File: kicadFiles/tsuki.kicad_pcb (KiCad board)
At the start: 2 copper layers, 283 x 94.2 mm, 194 parts, among them J1 TYPE-C-31-M12_13, J2 Conn_01x14, J3 Conn_01x14, SW1 ESC, SW10 9, SW11 0, SW12 -_, SW13 +=, SW14 2U BKSP, SW15 TAB_150, SW16 Q, SW17 W, SW18 E, SW19 R, SW2 1, SW20 T, SW21 Y, SW22 U, SW23 I, SW24 O, SW25 P, SW26 [{, SW27 ]}, SW28 \|_150, SW29 CAPS_175, SW3 2, SW30 A, SW31 S, SW32 D, SW33 F, SW34 G, SW35 H, SW36 J, SW37 K, SW38 L, SW39 :;, SW4 3, SW40 "', SW41 ENTER_225, SW42 LSHIFT_225, SW43 Z, SW44 X, SW45 C, SW46 V, SW47 B, SW48 N, SW49 M, SW5 4, SW50 <,, SW51 >., SW52 ?/, SW53 RSHIFT_275, SW54 LCTRL_150, SW55 LGUI_100, SW56 LALT_150, SW57 SPACE_600, SW58 RALT_150, SW59 RGUI_150, SW6 5, SW60 RCTRL_150, SW61 FN_100, SW62 RSHIFT_175, SW63 STEPPED_CAPS_125, SW64 1U LBKSP, SW65 1U RBKSP, SW66 ISO_100, SW67 ISO_ENTER, SW68 LCTRL_125, SW69 LGUI_125, SW7 6, SW70 LGUI_100, SW71 LALT_125, SW72 LALT_150, SW75 SPACE_625, SW77 SPACE_700, SW8 7, SW80 RALT_125, SW81 RALT_150, SW83 RGUI_125, SW84 RGUI_100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

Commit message: Added Schottky diodes and TVS
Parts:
- moved L4 20.3 mm to (250.9, 187.9)
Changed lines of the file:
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@@
     (mod_text_size 1 1)
     (mod_text_width 0.15)
-    (pad_size 3.9878 3.9878)
-    (pad_drill 3.9878)
+    (pad_size 10 4.500001)
+    (pad_drill 7.999999)
     (pad_to_mask_clearance 0.051)
     (solder_mask_min_width 0.25)
@@
     (fp_line (start -6 0) (end 6 0) (layer Cmts.User) (width 0.1))
     (fp_line (start 0 4) (end 0 -4) (layer Cmts.User) (width 0.1))
-    (pad "" thru_hole oval (at 0 0) (size 10 4.5) (drill oval 8 2.5) (layers *.Cu *.Mask))
+    (pad "" thru_hole oval (at 0 0) (size 10 4.500001) (drill oval 7.999999 2.5) (layers *.Cu *.Mask)
+      (clearance 1.016))
   )
   (module acheron_MountingHoles:MoutingHole_Oval_BackOnly_7mm_5.0x2.5mm (layer B.Cu)
@@
   )
   (module tsukiGraphics:tsukiLabel_30x12mm (layer F.Cu)
-    (at 250.92625 167.553125)
+    (at 250.92625 187.873125)
     (fp_text reference L4 (at 0 0) (layer F.Cu) hide
       (effects (font (size 1.524 1.524) (thickness 0.3)))
@@
   (module acheron_MountingHoles:MoutingHole_Oval_7mm_5.0x2.5mm (layer F.Cu)
     (at 279.50097 91.353125)
+    (clearance 1.016)
     (attr virtual)
     (fp_text reference H8 (at 0.1753 5.7861) (layer F.SilkS) hide
@@
     (fp_line (start -6 0) (end 6 0) (layer Cmts.User) (width 0.1))
     (fp_line (start 0 4) (end 0 -4) (layer Cmts.User) (width 0.1))
-    (pad "" thru_hole oval (at 0 0 180) (size 10 4.5) (drill oval 8 2.5) (layers *.Cu *.Mask))
+    (pad "" thru_hole oval (at 0 0 180) (size 10 4.500001) (drill oval 7.999999 2.5) (layers *.Cu *.Mask)
+      (clearance 1.016))
   )
   (module acheron_Components:D_SOD-123 (layer F.Cu)

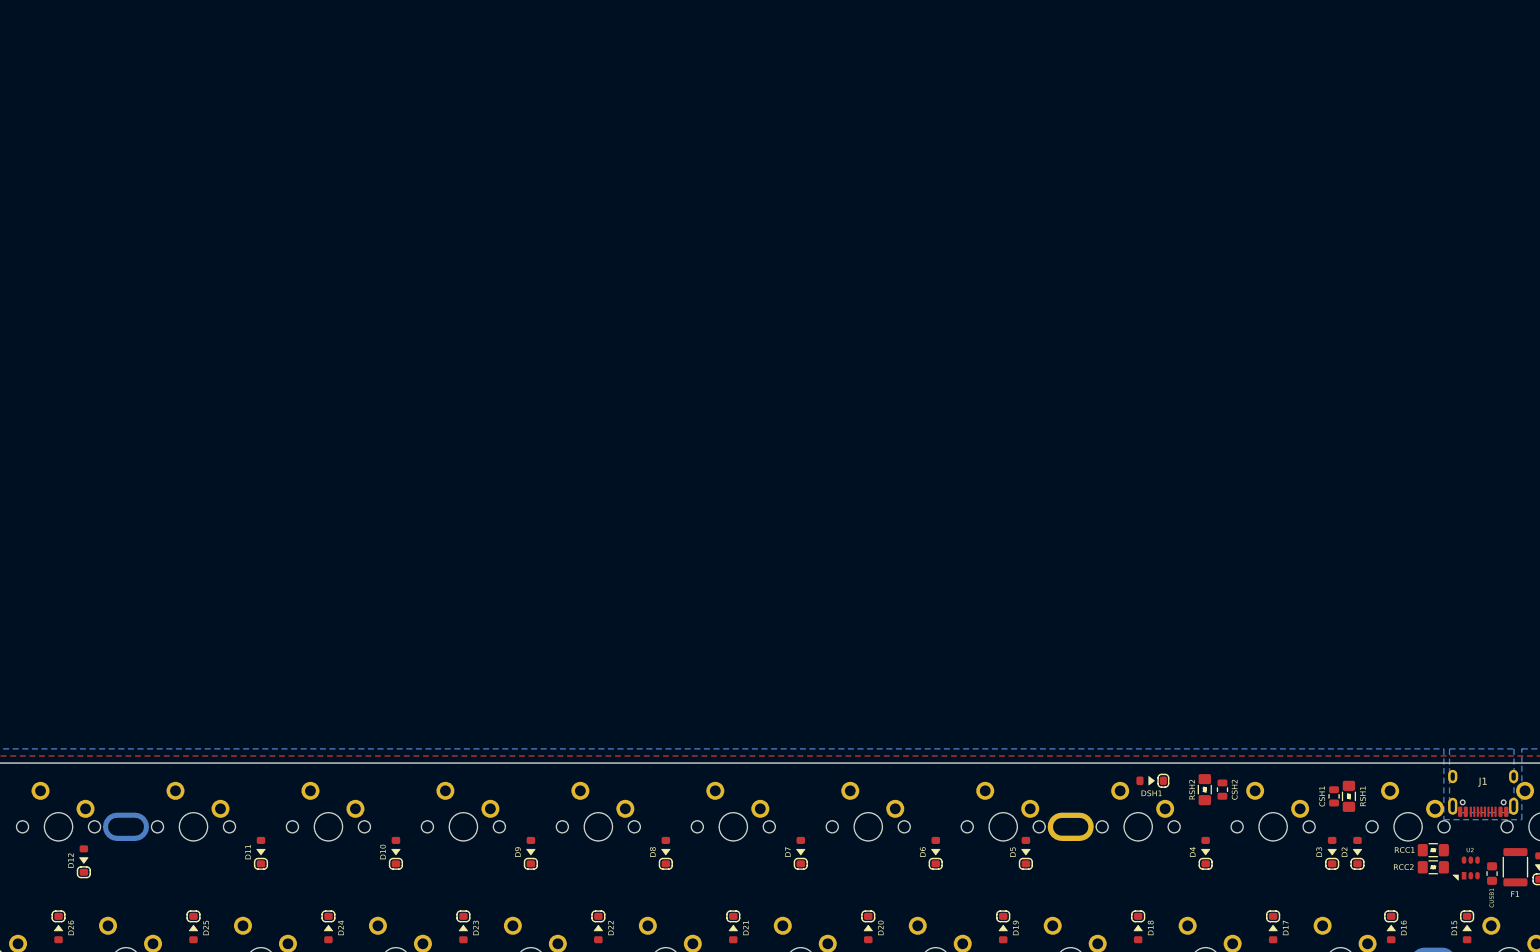
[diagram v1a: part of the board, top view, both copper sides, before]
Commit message: Added RGB to schematic
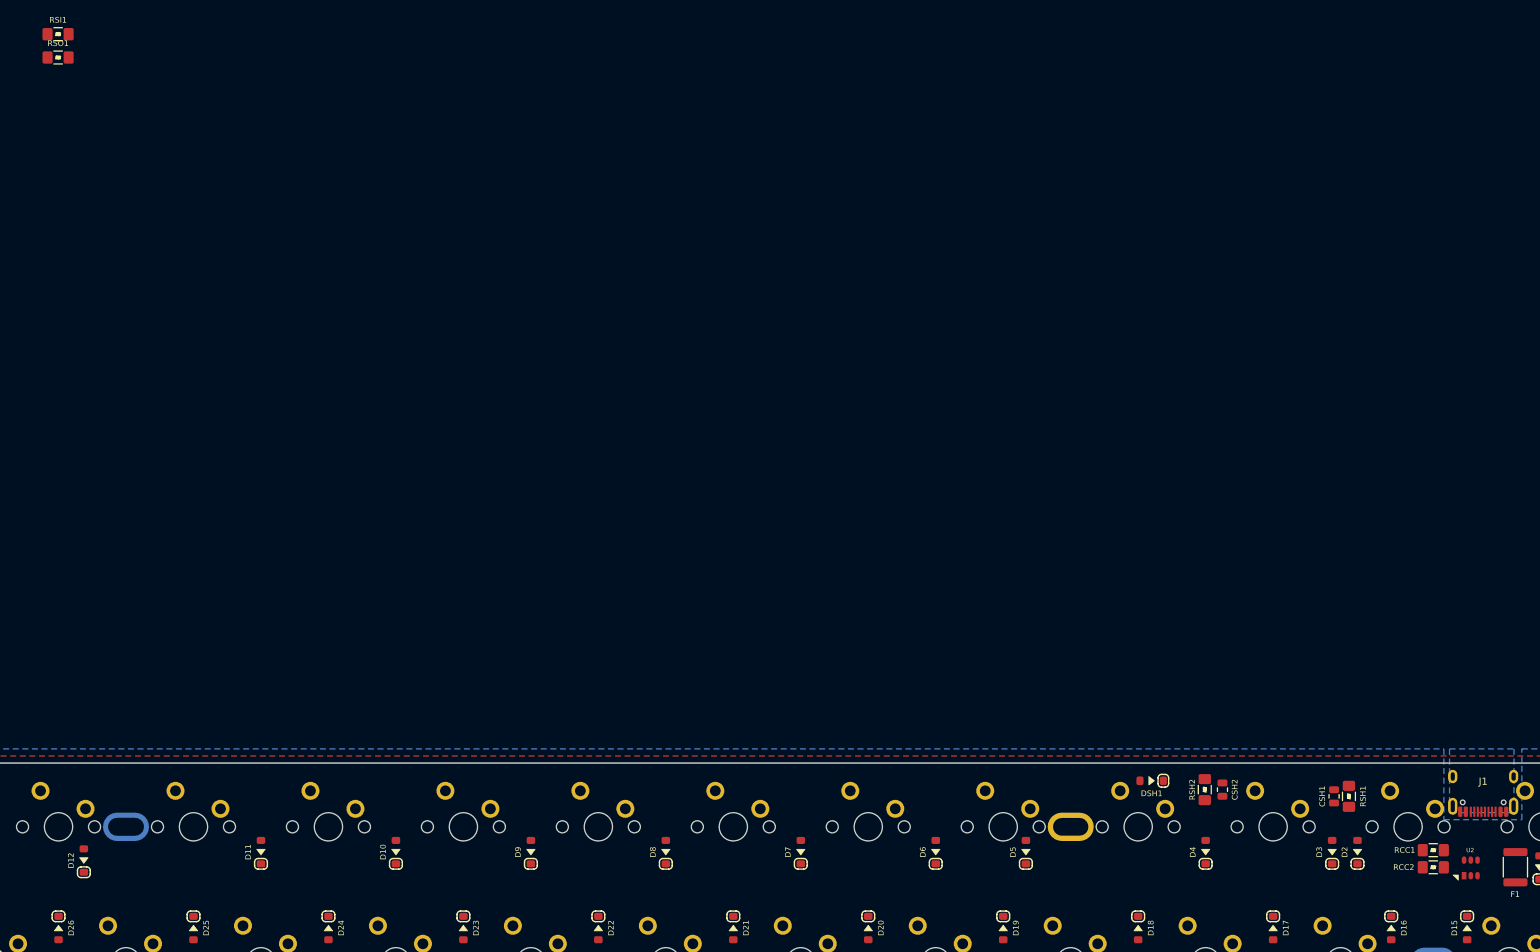
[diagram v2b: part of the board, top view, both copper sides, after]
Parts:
- removed CUSB1: 100n, Capacitor_SMD:C_0805_2012Metric_Pad1.15x1.40mm_HandSolder
- added RSI1: 100k, acheron_Components:R_SMD_1206, F.Cu at (136.6, -20.5)
- added RSO1: 100k, acheron_Components:R_SMD_1206, F.Cu at (136.6, -17.2)
- CSI1, CSO1: value 100n -> 1u
- DF1: value RB060M-60TR -> SMF9.0CA
- DS1: value 1N4148 -> RB060M-60TR
- DSH1: value 1N4007 -> RB060M-60TR
- J3: value Conn_01x14 -> Conn_ARM_JTAG_SWD_10
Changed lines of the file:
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@@
     (tracks 0)
     (zones 0)
-    (modules 194)
+    (modules 195)
     (nets 122)
   )
@@
     (add_net D-)
   )
+  (module acheron_Components:R_SMD_1206 (layer F.Cu)
+    (at 136.561251 -17.241874)
+    (descr "Resistor SMD 1206 (3216 Metric), square (rectangular) end terminal, IPC_7351 nominal with elongated pad for handsoldering. (Body size source: http://www.tortai-tech.com/upload/download/2011102023233369053.pdf), generated with kicad-footprint-generator")
+    (tags "resistor handsolder")
+    (attr smd)
+    (fp_text reference RSO1 (at 0 -2) (layer F.SilkS)
+      (effects (font (size 0.8 0.8) (thickness 0.2)))
+    )
+    (fp_text value 100k (at 0 2) (layer F.Fab)
+      (effects (font (size 0.6 0.6) (thickness 0.1)))
+    )
+    (fp_line (start 0.25 0.2) (end 0.35 -0.2) (layer F.SilkS) (width 0.1))
+    (fp_line (start 0.15 -0.2) (end 0.25 0.2) (layer F.SilkS) (width 0.1))
+    (fp_line (start 0.05 0.2) (end 0.15 -0.2) (layer F.SilkS) (width 0.1))
+    (fp_line (start -0.05 -0.2) (end 0.05 0.2) (layer F.SilkS) (width 0.1))
+    (fp_line (start -0.15 0.2) (end -0.05 -0.2) (layer F.SilkS) (width 0.1))
+    (fp_line (start -0.25 -0.2) (end -0.15 0.2) (layer F.SilkS) (width 0.1))
+    (fp_line (start -0.35 0.2) (end -0.25 -0.2) (layer F.SilkS) (width 0.1))
+    (fp_text user %R (at 0 0) (layer F.Fab)
+      (effects (font (size 0.6 0.6) (thickness 0.15)))
+    )
+    (fp_line (start 2.45 1.12) (end -2.45 1.12) (layer F.CrtYd) (width 0.05))
+    (fp_line (start 2.45 -1.12) (end 2.45 1.12) (layer F.CrtYd) (width 0.05))
+    (fp_line (start -2.45 -1.12) (end 2.45 -1.12) (layer F.CrtYd) (width 0.05))
+    (fp_line (start -2.45 1.12) (end -2.45 -1.12) (layer F.CrtYd) (width 0.05))
+    (fp_line (start -0.602064 0.91) (end 0.602064 0.91) (layer F.SilkS) (width 0.12))
+    (fp_line (start -0.602064 -0.91) (end 0.602064 -0.91) (layer F.SilkS) (width 0.12))
+    (fp_line (start 1.6 0.8) (end -1.6 0.8) (layer F.Fab) (width 0.1))
+    (fp_line (start 1.6 -0.8) (end 1.6 0.8) (layer F.Fab) (width 0.1))
+    (fp_line (start -1.6 -0.8) (end 1.6 -0.8) (layer F.Fab) (width 0.1))
+    (fp_line (start -1.6 0.8) (end -1.6 -0.8) (layer F.Fab) (width 0.1))
+    (pad 2 smd roundrect (at 1.4875 0) (size 1.425 1.75) (layers F.Cu F.Paste F.Mask) (roundrect_rratio 0.175439)
+      (net 2 GND))
+    (pad 1 smd roundrect (at -1.4875 0) (size 1.425 1.75) (layers F.Cu F.Paste F.Mask) (roundrect_rratio 0.175439)
+      (net 1 3.3V))
+    (model ${KISYS3DMOD}/Resistor_SMD.3dshapes/R_1206_3216Metric.wrl
+      (at (xyz 0 0 0))
+      (scale (xyz 1 1 1))
+      (rotate (xyz 0 0 0))
+    )
+  )
+  (module acheron_Components:R_SMD_1206 (layer F.Cu)
+    (at 136.561251 -20.531874)
+    (descr "Resistor SMD 1206 (3216 Metric), square (rectangular) end terminal, IPC_7351 nominal with elongated pad for handsoldering. (Body size source: http://www.tortai-tech.com/upload/download/2011102023233369053.pdf), generated with kicad-footprint-generator")
+    (tags "resistor handsolder")
+    (attr smd)
+    (fp_text reference RSI1 (at 0 -2) (layer F.SilkS)
+      (effects (font (size 0.8 0.8) (thickness 0.2)))
+    )
+    (fp_text value 100k (at 0 2) (layer F.Fab)
+      (effects (font (size 0.6 0.6) (thickness 0.1)))
+    )
+    (fp_line (start 0.25 0.2) (end 0.35 -0.2) (layer F.SilkS) (width 0.1))
+    (fp_line (start 0.15 -0.2) (end 0.25 0.2) (layer F.SilkS) (width 0.1))
+    (fp_line (start 0.05 0.2) (end 0.15 -0.2) (layer F.SilkS) (width 0.1))
+    (fp_line (start -0.05 -0.2) (end 0.05 0.2) (layer F.SilkS) (width 0.1))
+    (fp_line (start -0.15 0.2) (end -0.05 -0.2) (layer F.SilkS) (width 0.1))
+    (fp_line (start -0.25 -0.2) (end -0.15 0.2) (layer F.SilkS) (width 0.1))
+    (fp_line (start -0.35 0.2) (end -0.25 -0.2) (layer F.SilkS) (width 0.1))
+    (fp_text user %R (at 0 0) (layer F.Fab)
+      (effects (font (size 0.6 0.6) (thickness 0.15)))
+    )
+    (fp_line (start 2.45 1.12) (end -2.45 1.12) (layer F.CrtYd) (width 0.05))
+    (fp_line (start 2.45 -1.12) (end 2.45 1.12) (layer F.CrtYd) (width 0.05))
+    (fp_line (start -2.45 -1.12) (end 2.45 -1.12) (layer F.CrtYd) (width 0.05))
+    (fp_line (start -2.45 1.12) (end -2.45 -1.12) (layer F.CrtYd) (width 0.05))
+    (fp_line (start -0.602064 0.91) (end 0.602064 0.91) (layer F.SilkS) (width 0.12))
+    (fp_line (start -0.602064 -0.91) (end 0.602064 -0.91) (layer F.SilkS) (width 0.12))
+    (fp_line (start 1.6 0.8) (end -1.6 0.8) (layer F.Fab) (width 0.1))
+    (fp_line (start 1.6 -0.8) (end 1.6 0.8) (layer F.Fab) (width 0.1))
+    (fp_line (start -1.6 -0.8) (end 1.6 -0.8) (layer F.Fab) (width 0.1))
+    (fp_line (start -1.6 0.8) (end -1.6 -0.8) (layer F.Fab) (width 0.1))
+    (pad 2 smd roundrect (at 1.4875 0) (size 1.425 1.75) (layers F.Cu F.Paste F.Mask) (roundrect_rratio 0.175439)
+      (net 2 GND))
+    (pad 1 smd roundrect (at -1.4875 0) (size 1.425 1.75) (layers F.Cu F.Paste F.Mask) (roundrect_rratio 0.175439)
+      (net 6 5V))
+    (model ${KISYS3DMOD}/Resistor_SMD.3dshapes/R_1206_3216Metric.wrl
+      (at (xyz 0 0 0))
+      (scale (xyz 1 1 1))
+      (rotate (xyz 0 0 0))
+    )
+  )
   (module acheron_MountingHoles:MoutingHole_Oval_BackOnly_7mm_5.0x2.5mm (layer B.Cu)
     (at 95.32625 110.403205 180)
@@
       (effects (font (size 1 1) (thickness 0.15)))
     )
-    (fp_text value Conn_01x14 (at 4.064 0 90) (layer F.Fab) hide
+    (fp_text value Conn_ARM_JTAG_SWD_10 (at 4.064 0 90) (layer F.Fab) hide
       (effects (font (size 1 1) (thickness 0.15)))
     )
@@
       (effects (font (size 0.8 0.8) (thickness 0.2)))
     )
-    (fp_text value 1N4007 (at 0 1.524) (layer F.Fab)
+    (fp_text value RB060M-60TR (at 0 1.524) (layer F.Fab)
       (effects (font (size 0.5 0.5) (thickness 0.125)))
     )
@@
       (effects (font (size 0.8 0.8) (thickness 0.2)))
     )
-    (fp_text value 1N4148 (at 0 2.41 90) (layer F.Fab)
+    (fp_text value RB060M-60TR (at 0 2.41 90) (layer F.Fab)
       (effects (font (size 0.5 0.5) (thickness 0.125)))
     )
@@
       (effects (font (size 0.8 0.8) (thickness 0.2)))
     )
-    (fp_text value RB060M-60TR (at 0 1.524 90) (layer F.Fab)
+    (fp_text value SMF9.0CA (at 0 1.524 90) (layer F.Fab)
       (effects (font (size 0.5 0.5) (thickness 0.125)))
     )
@@
   )
   (module Capacitor_SMD:C_0805_2012Metric_Pad1.15x1.40mm_HandSolder (layer F.Cu)
-    (at 338.97625 97.953125 90)
-    (descr "Capacitor SMD 0805 (2012 Metric), square (rectangular) end terminal, IPC_7351 nominal with elongated pad for handsoldering. (Body size source: https://docs.google.com/spreadsheets/d/1BsfQQcO9C6DZCsRaXUlFlo91Tg2WpOkGARC1WS5S8t0/edit?usp=sharing), generated with kicad-footprint-generator")
-    (tags "capacitor handsolder")
-    (attr smd)
-    (fp_text reference CUSB1 (at -3.433 -0.039 90) (layer F.SilkS)
-      (effects (font (size 0.6 0.6) (thickness 0.12)))
-    )
-    (fp_text value 100n (at -2.036 0.088 90) (layer F.Fab)
-      (effects (font (size 0.5 0.5) (thickness 0.1)))
-    )
-    (fp_text user %R (at 0 0 90) (layer F.Fab)
-      (effects (font (size 0.3 0.3) (thickness 0.075)))
-    )
-    (fp_line (start 1.85 0.95) (end -1.85 0.95) (layer F.CrtYd) (width 0.05))
-    (fp_line (start 1.85 -0.95) (end 1.85 0.95) (layer F.CrtYd) (width 0.05))
-    (fp_line (start -1.85 -0.95) (end 1.85 -0.95) (layer F.CrtYd) (width 0.05))
-    (fp_line (start -1.85 0.95) (end -1.85 -0.95) (layer F.CrtYd) (width 0.05))
-    (fp_line (start -0.261252 0.71) (end 0.261252 0.71) (layer F.SilkS) (width 0.12))
-    (fp_line (start -0.261252 -0.71) (end 0.261252 -0.71) (layer F.SilkS) (width 0.12))
-    (fp_line (start 1 0.6) (end -1 0.6) (layer F.Fab) (width 0.1))
-    (fp_line (start 1 -0.6) (end 1 0.6) (layer F.Fab) (width 0.1))
-    (fp_line (start -1 -0.6) (end 1 -0.6) (layer F.Fab) (width 0.1))
-    (fp_line (start -1 0.6) (end -1 -0.6) (layer F.Fab) (width 0.1))
-    (pad 2 smd roundrect (at 1.025 0 90) (size 1.15 1.4) (layers F.Cu F.Paste F.Mask) (roundrect_rratio 0.217391)
-      (net 7 VBUS))
-    (pad 1 smd roundrect (at -1.025 0 90) (size 1.15 1.4) (layers F.Cu F.Paste F.Mask) (roundrect_rratio 0.217391)
-      (net 2 GND))
-    (model ${KISYS3DMOD}/Capacitor_SMD.3dshapes/C_0805_2012Metric.wrl
-      (at (xyz 0 0 0))
-      (scale (xyz 1 1 1))
-      (rotate (xyz 0 0 0))
-    )
-  )
-  (module Capacitor_SMD:C_0805_2012Metric_Pad1.15x1.40mm_HandSolder (layer F.Cu)
     (at 318.87625 153.353125 180)
     (descr "Capacitor SMD 0805 (2012 Metric), square (rectangular) end terminal, IPC_7351 nominal with elongated pad for handsoldering. (Body size source: https://docs.google.com/spreadsheets/d/1BsfQQcO9C6DZCsRaXUlFlo91Tg2WpOkGARC1WS5S8t0/edit?usp=sharing), generated with kicad-footprint-generator")
@@
       (effects (font (size 0.6 0.6) (thickness 0.12)))
     )
-    (fp_text value 100n (at 0 -1.246) (layer F.Fab)
+    (fp_text value 1u (at 0 -1.246) (layer F.Fab)
       (effects (font (size 0.5 0.5) (thickness 0.1)))
     )
@@
       (effects (font (size 0.6 0.6) (thickness 0.12)))
     )
-    (fp_text value 100n (at 0 -1.368) (layer F.Fab)
+    (fp_text value 1u (at 0 -1.368) (layer F.Fab)
       (effects (font (size 0.5 0.5) (thickness 0.1)))
     )

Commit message: Added LED control to schematic
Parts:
- removed SW57: SPACE_600, acheron_MX_SolderMask:MX600R
- added CRGB1: 100n, Capacitor_SMD:C_0805_2012Metric, F.Cu at (303.3, 100.9)
- added CRGB10: 100n, Capacitor_SMD:C_0805_2012Metric, F.Cu at (470.6, 187.0)
- added CRGB2: 100n, Capacitor_SMD:C_0805_2012Metric, F.Cu at (256.6, 101.6)
- added CRGB3: 100n, Capacitor_SMD:C_0805_2012Metric, F.Cu at (466.6, 196.6)
- added CRGB4: 100n, Capacitor_SMD:C_0805_2012Metric, F.Cu at (462.2, 201.1)
- added CRGB5: 100n, Capacitor_SMD:C_0805_2012Metric, F.Cu at (471.1, 190.0)
- added CRGB6: 100n, Capacitor_SMD:C_0805_2012Metric, F.Cu at (466.7, 193.6)
- added CRGB7: 100n, Capacitor_SMD:C_0805_2012Metric, F.Cu at (462.2, 198.2)
- added CRGB8: 100n, Capacitor_SMD:C_0805_2012Metric, F.Cu at (462.2, 195.2)
- added CRGB9: 100n, Capacitor_SMD:C_0805_2012Metric, F.Cu at (466.7, 190.7)
- added Q1: BSS138, Package_TO_SOT_SMD:SOT-23, F.Cu at (451.0, 191.4)
- added RGB1: WS2812B, acheron_Components:LED_WS2812B_5.0x5.0mm_P3.2mm, F.Cu at (308.1, 100.9)
- added RGB10: WS2812B, acheron_Components:LED_WS2812B_5.0x5.0mm_P3.2mm, F.Cu at (305.7, 158.0)
- added RGB2: WS2812B, acheron_Components:LED_WS2812B_5.0x5.0mm_P3.2mm, F.Cu at (262.8, 100.9)
- added RGB3: WS2812B, acheron_Components:LED_WS2812B_5.0x5.0mm_P3.2mm, F.Cu at (212.8, 100.9)
- added RGB4: WS2812B, acheron_Components:LED_WS2812B_5.0x5.0mm_P3.2mm, F.Cu at (167.6, 100.9)
- added RGB5: WS2812B, acheron_Components:LED_WS2812B_5.0x5.0mm_P3.2mm, F.Cu at (117.6, 100.9)
- added RGB6: WS2812B, acheron_Components:LED_WS2812B_5.0x5.0mm_P3.2mm, F.Cu at (117.6, 158.0)
- added RGB7: WS2812B, acheron_Components:LED_WS2812B_5.0x5.0mm_P3.2mm, F.Cu at (165.2, 158.0)
- added RGB8: WS2812B, acheron_Components:LED_WS2812B_5.0x5.0mm_P3.2mm, F.Cu at (215.2, 158.0)
- added RGB9: WS2812B, acheron_Components:LED_WS2812B_5.0x5.0mm_P3.2mm, F.Cu at (262.8, 158.0)
- added RRGB1: 5.1R, acheron_Components:R_SMD_1206, F.Cu at (301.0, 100.9)
- added RRGB10: 5.1R, acheron_Components:R_SMD_1206, F.Cu at (474.5, 132.0)
- added RRGB2: 5.1R, acheron_Components:R_SMD_1206, F.Cu at (254.4, 100.9)
- added RRGB3: 5.1R, acheron_Components:R_SMD_1206, F.Cu at (462.6, 132.0)
- added RRGB4: 5.1R, acheron_Components:R_SMD_1206, F.Cu at (456.7, 138.6)
- added RRGB5: 5.1R, acheron_Components:R_SMD_1206, F.Cu at (462.6, 135.3)
- added RRGB6: 5.1R, acheron_Components:R_SMD_1206, F.Cu at (468.6, 132.0)
- added RRGB7: 5.1R, acheron_Components:R_SMD_1206, F.Cu at (456.7, 141.9)
- added RRGB8: 5.1R, acheron_Components:R_SMD_1206, F.Cu at (462.6, 138.6)
- added RRGB9: 5.1R, acheron_Components:R_SMD_1206, F.Cu at (468.6, 135.3)
- added RS1: 10k, acheron_Components:R_SMD_1206, F.Cu at (446.2, 191.4)
- added RS2: 10k, acheron_Components:R_SMD_1206, F.Cu at (455.7, 191.4)
- RCC1, RCC2, RRST1, RSH1, RSH2: footprint acheron_Components:R_SMD_1026 -> acheron_Components:R_SMD_1206
- moved RSI1 244.0 mm to (340.2, 114.0)
- moved RSO1 244.0 mm to (340.2, 117.3)
- moved J3 148.2 mm to (183.1, 167.6)
- moved CSI1 129.0 mm to (190.8, 161.6), turned to 90 degrees
- moved RRST1 127.8 mm to (197.0, 155.6), turned to 0 degrees
- moved DRST1 125.2 mm to (197.1, 158.2), turned to 0 degrees
- moved SWRST1 120.2 mm to (195.0, 166.4), turned to 0 degrees
- moved QRST1 113.7 mm to (197.1, 171.2), turned to 270 degrees
- moved CRST2 111.2 mm to (196.2, 174.7), turned to 0 degrees
- moved CSO1 45.3 mm to (339.0, 112.8), turned to 270 degrees
- moved CRST1 39.7 mm to (342.4, 115.2), turned to 180 degrees
- moved U3 39.3 mm to (341.4, 117.5), turned to 90 degrees
- moved D59 21.5 mm to (98.5, 160.4)
- moved D55 21.4 mm to (327.1, 160.4)
- moved D56 15.5 mm to (286.6, 160.4)
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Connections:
- U1 pad 41: Extra1 -> RGB_3V3
